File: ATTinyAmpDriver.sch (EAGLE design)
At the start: 28 parts, among them Q1 SI2301CDS, Q2 BC846, U1 SPX5205M5-L-3-3, U2 ATTINY5-TSHR, U3 MCP6L2-X_SN, X1 DIODES, X2 INPUT

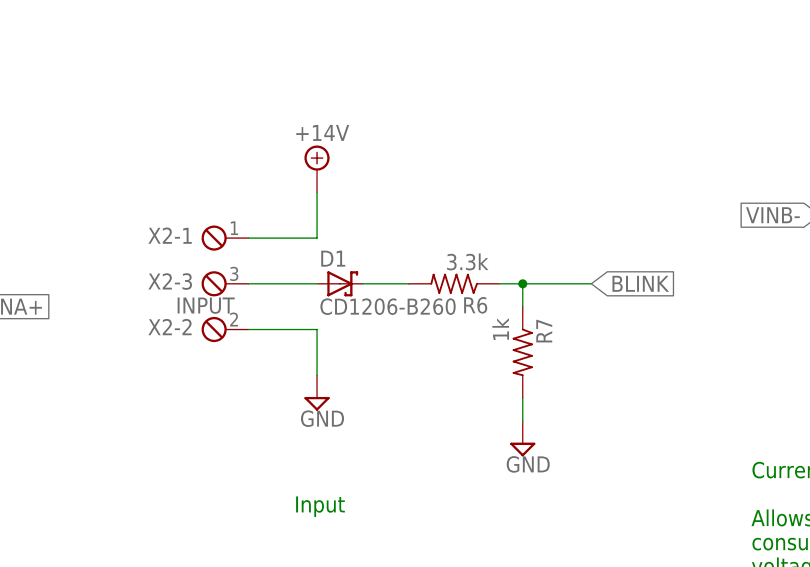
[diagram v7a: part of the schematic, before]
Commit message: Changed blink diode to regular rectifier diode
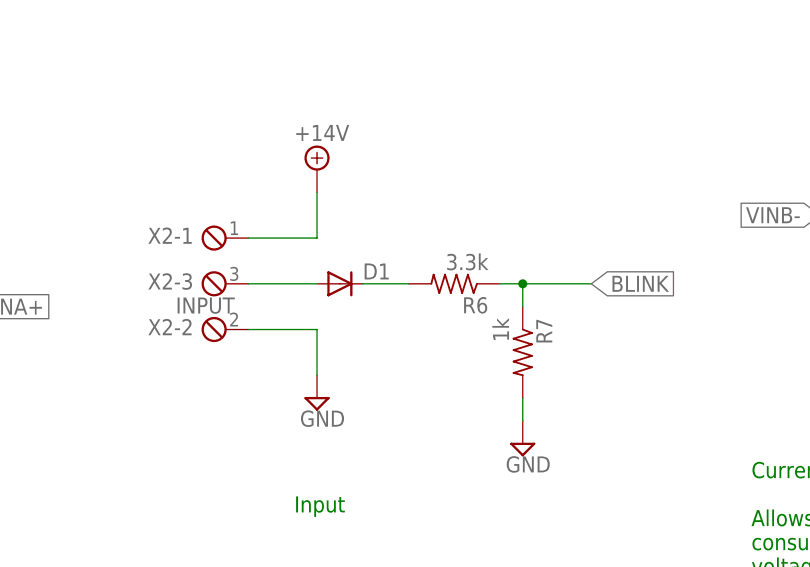
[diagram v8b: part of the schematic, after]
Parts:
- D1: value CD1206-B260 -> DIODE_0603; device Combined:CD1206-B260 -> Combined:DIODE_0603; DIGIKEY CD1206-B260CT-ND -> 641-1002-1-ND; DIGIKEY_COST .49 -> .23
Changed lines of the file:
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@@
 </part>
 <part name="SUPPLY22" library="supply2" deviceset="GND" device=""/>
-<part name="D1" library="Combined" deviceset="CD1206-B260" device="">
-<attribute name="DIGIKEY" value="CD1206-B260CT-ND"/>
-<attribute name="DIGIKEY_COST" value=".49"/>
+<part name="D1" library="Combined" deviceset="DIODE_0603" device="">
+<attribute name="DIGIKEY" value="641-1002-1-ND"/>
+<attribute name="DIGIKEY_COST" value=".23"/>
 </part>
 <part name="R8" library="resistor" deviceset="R-US_" device="R0603" value="1k">
@@
 </instance>
 <instance part="SUPPLY22" gate="GND" x="243.84" y="35.56"/>
-<instance part="D1" gate="G$1" x="167.64" y="124.46">
+<instance part="D1" gate="G$1" x="167.64" y="124.46" smashed="yes">
 <attribute name="DIGIKEY" x="167.64" y="124.46" size="1.778" layer="96" display="off"/>
 <attribute name="DIGIKEY_COST" x="167.64" y="124.46" size="1.778" layer="96" display="off"/>
+<attribute name="NAME" x="170.18" y="124.9426" size="1.778" layer="95"/>
 </instance>
 <instance part="R8" gate="G$1" x="228.6" y="124.46" rot="MR270">
